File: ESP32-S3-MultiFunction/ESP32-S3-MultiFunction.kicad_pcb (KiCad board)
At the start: 2 copper layers, 99.1 x 125.7 mm, 140 parts, among them IC1 ESP32-S3-WROOM-1U-N8, IC2 USBLC6-2SC6, J1 USB_C, J501 -SM+, J801 RJ45, J802 RJ45, P701 A7 A6 A5 A4 A3 A2 A1 A0 C, P702 B7 B6 B5 B4 B3 B2 B1 B0 C, SW1 BOOT, SW201 RESET, T701 + 12V -, T801 - 15 in +, T802 - 15 out +, U301 LM2574N-3.3, U401 TC4426, U402 TC4426, U403 74HCT14, U501 74HCT00, U502 74HCT00, U503 TC4428, U504 TC4428, U505 TC4428, U506 TC4428, U601 LM339, U602 LM339, U701 PCA9685, U702 TBD62X83A, U703 TBD62X83A, U801 TCAN332DR

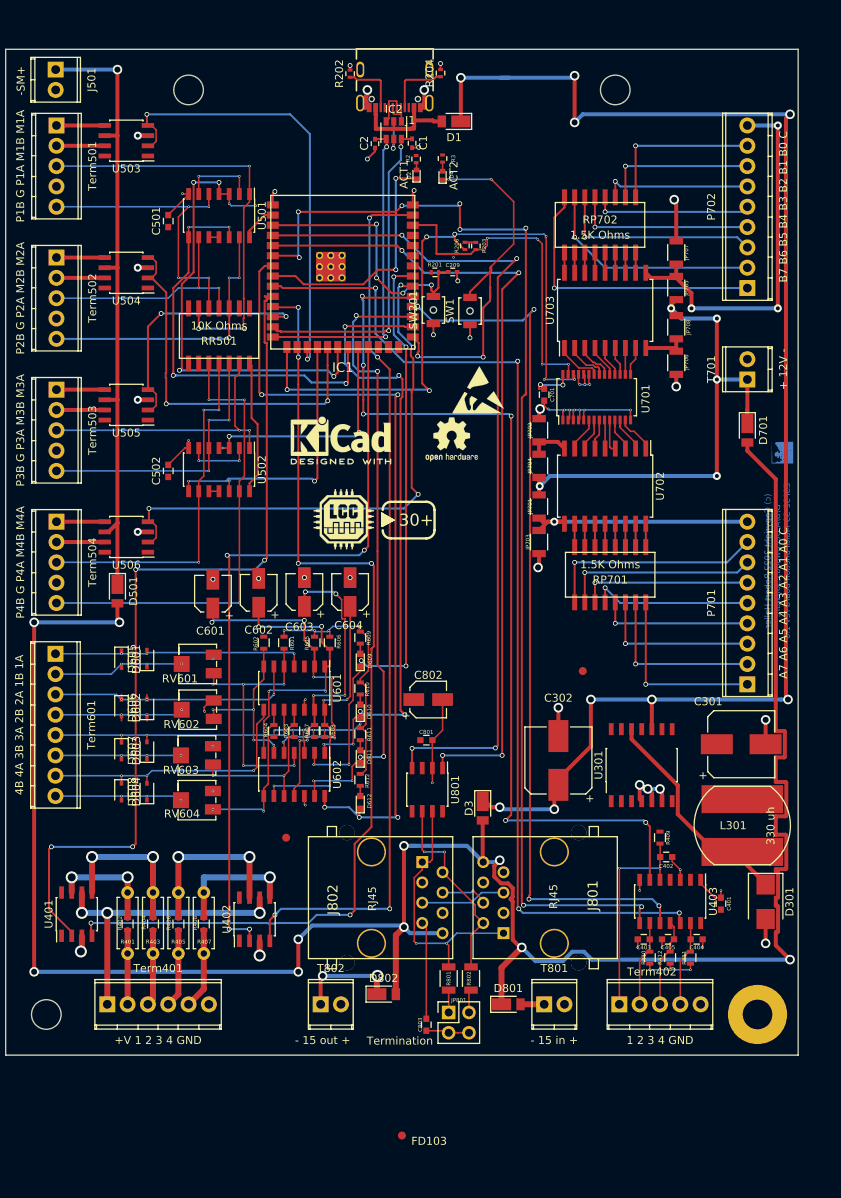
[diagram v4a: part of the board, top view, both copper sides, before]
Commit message: Revert to chip version, USB-C, replace reset and boot buttons.
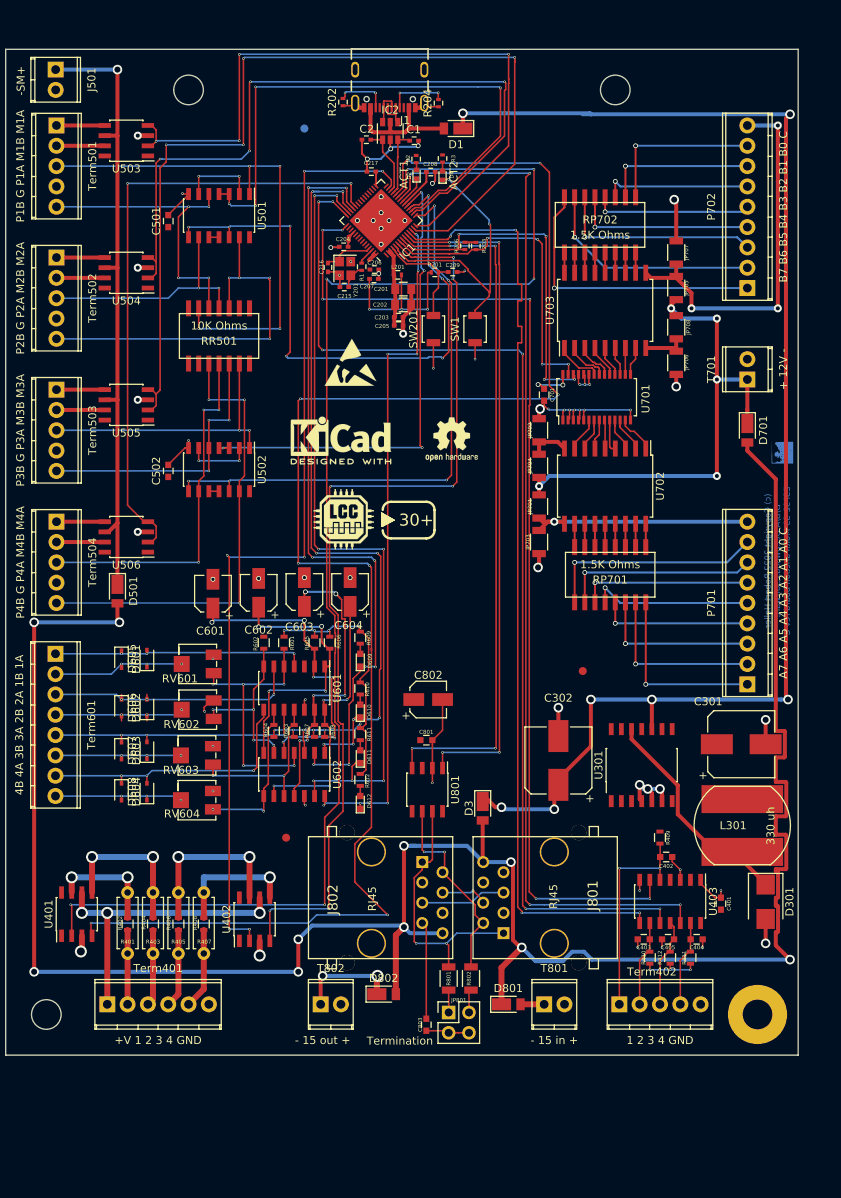
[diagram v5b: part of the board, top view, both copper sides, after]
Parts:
- added C201: 10uf, Capacitors_SMD:C_0805, F.Cu at (123.4, 55.4)
- added C202: 10uf, Capacitors_SMD:C_0805, F.Cu at (123.3, 57.4)
- added C203: 1uf, Capacitors_SMD:C_0402, F.Cu at (122.8, 58.9)
- added C204: 100nf, Capacitors_SMD:C_0402, F.Cu at (115.9, 50.1)
- added C205: 100nf, Capacitors_SMD:C_0402, F.Cu at (122.8, 59.9)
- added C206: 1uf, Capacitors_SMD:C_0402, F.Cu at (119.7, 52.9)
- added C207: 100pf, Capacitors_SMD:C_0402, F.Cu at (119.7, 54.1)
- added C208: 100nf, Capacitors_SMD:C_0402, F.Cu at (126.8, 40.7)
- added C215: 22pf, Capacitors_SMD:C_0402, F.Cu at (116.0, 55.1)
- added C216: 22pf, Capacitors_SMD:C_0402, F.Cu at (113.9, 52.7)
- added C217: 1uf, Capacitors_SMD:C_0402, F.Cu at (119.4, 40.7)
- added L201: 2.0nH, Inductors_SMD:L_0402, F.Cu at (122.7, 53.6)
- added R1: 0, Resistors_SMD:R_0402, F.Cu at (118.2, 52.6)
- added Y201: 40 Mhz +/- 10 ppm, FA_20H:FA20_H, F.Cu at (116.1, 52.8)
- FD103: moved to B.Cu
- IC1: value ESP32-S3-WROOM-1U-N8 -> ESP32-S3FN8; footprint ESP32-S3-WROOM:ESP32_S3_WROOM-1U -> Housings_DFN_QFN:QFN-56-1EP_7x7mm_Pitch0.4mm
- SW1, SW201: footprint Buttons_Switches_SMD:SW_SPST_B3U-1000P-B -> Buttons_Switches_SMD:SW_SPST_B3U-1000P
- moved FD103 126.5 mm to (111.0, 35.3)
- moved REF*** 16.3 mm to (116.8, 64.5)
- moved IC1 8.43 mm to (120.6, 46.8), turned to 135 degrees
- moved R204 3.76 mm to (127.8, 32.1)
- moved R202 3.67 mm to (115.8, 32.0)
- moved SW201 2.38 mm to (127.1, 60.4)
- moved SW1 2.34 mm to (132.3, 60.4)
- moved C2 1.18 mm to (118.7, 36.7), turned to 180 degrees
- moved D1 0.92 mm to (130.0, 35.3)
- moved J1 0.64 mm to (121.7, 28.0)
- moved IC2 0.45 mm to (121.7, 35.6)
- moved C1 0.41 mm to (124.7, 36.8), turned to 180 degrees
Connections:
- D609 pad 1: /ESP32 MCU/GPIO40(OD1) -> /ESP32 MCU/GPIO34(OD1)
- IC1 pad 1: GND -> Net-(IC1-Pad1)
- IC1 pad 10: /ESP32 MCU/GPIO17(LEDS1) -> /CAN Tranceiver/CAN_TX
- IC1 pad 11: /ESP32 MCU/GPIO18(LEDS2) -> /Buttons and LEDs/Button2
- IC1 pad 12: /ESP32 MCU/GPIO8(Motor3) -> /ESP32 MCU/GPIO7(OD4)
- IC1 pad 13: /ESP32 MCU/D- -> /ESP32 MCU/GPIO8(Motor3)
- IC1 pad 14: /ESP32 MCU/D+ -> /ESP32 MCU/GPIO9(Motor1)
- IC1 pad 15: /ESP32 MCU/SCL -> /ESP32 MCU/GPIO10(Points4)
- IC1 pad 16: Net-(IC1-Pad16) -> /ESP32 MCU/GPIO11(Motor2)
- IC1 pad 17: /ESP32 MCU/GPIO9(Motor1) -> /ESP32 MCU/GPIO12(Points1)
- IC1 pad 18: /ESP32 MCU/GPIO10(Points4) -> /ESP32 MCU/GPIO13(Points2)
- IC1 pad 19: /ESP32 MCU/GPIO11(Motor2) -> /ESP32 MCU/GPIO14(Points3)
- IC1 pad 2: +3V3 -> /ESP32 MCU/VDD3P3
- IC1 pad 20: /ESP32 MCU/GPIO12(Points1) -> +3V3
- IC1 pad 21: /ESP32 MCU/GPIO13(Points2) -> /ESP32 MCU/GPIO15(Act1)
- IC1 pad 22: /ESP32 MCU/GPIO14(Points3) -> /Buttons and LEDs/Button4
- IC1 pad 23: /ESP32 MCU/GPIO21(LEDS3) -> /ESP32 MCU/GPIO17(LEDS1)
- IC1 pad 24: Net-(IC1-Pad24) -> /ESP32 MCU/GPIO18(LEDS2)
- IC1 pad 25: Net-(IC1-Pad25) -> /ESP32 MCU/D-
- IC1 pad 26: Net-(IC1-Pad26) -> /ESP32 MCU/D+
- IC1 pad 27: /ESP32 MCU/GPIO0(Act2) -> /ESP32 MCU/GPIO21(LEDS3)
- IC1 pad 28: /ESP32 MCU/GPIO35(OD2) -> Net-(IC1-Pad28)
- IC1 pad 29: /ESP32 MCU/GPIO36(OD3) -> Net-(C217-Pad1)
- IC1 pad 3: /ESP32 MCU/RESET -> /ESP32 MCU/VDD3P3
- IC1 pad 30: /Buttons and LEDs/Button3 -> Net-(IC1-Pad30)
- IC1 pad 31: /Buttons and LEDs/Button1 -> Net-(IC1-Pad31)
- IC1 pad 32: /ESP32 MCU/GPIO39(Motor4) -> Net-(IC1-Pad32)
- IC1 pad 33: /ESP32 MCU/GPIO40(OD1) -> Net-(IC1-Pad33)
- IC1 pad 38: /ESP32 MCU/SDA -> /ESP32 MCU/GPIO33(Motor4)
- IC1 pad 39: /ESP32 MCU/GPIO1(LEDS4) -> /ESP32 MCU/GPIO34(OD1)
- IC1 pad 4: /CAN Tranceiver/CAN_RX -> /ESP32 MCU/RESET
- IC1 pad 40: GND -> /ESP32 MCU/GPIO35(OD2)
- IC1 pad 5: /CAN Tranceiver/CAN_TX -> /ESP32 MCU/GPIO0(Act2)
- IC1 pad 6: /Buttons and LEDs/Button2 -> /ESP32 MCU/GPIO1(LEDS4)
- IC1 pad 7: /ESP32 MCU/GPIO7(OD4) -> /ESP32 MCU/SDA
- IC1 pad 8: /ESP32 MCU/GPIO15(Act1) -> /ESP32 MCU/SCL
- IC1 pad 9: /Buttons and LEDs/Button4 -> /CAN Tranceiver/CAN_RX
- R202 pad 1: Net-(J1-PadB5) -> GND
- R202 pad 2: GND -> Net-(J1-PadB5)
- R204 pad 1: Net-(J1-PadA5) -> GND
- R204 pad 2: GND -> Net-(J1-PadA5)
- U506 pad 2: /ESP32 MCU/GPIO39(Motor4) -> /ESP32 MCU/GPIO33(Motor4)
- U506 pad 4: /ESP32 MCU/GPIO39(Motor4) -> /ESP32 MCU/GPIO33(Motor4)
- U602 pad 2: /ESP32 MCU/GPIO40(OD1) -> /ESP32 MCU/GPIO34(OD1)
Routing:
- net /ESP32 MCU/GPIO34(OD1): track 0.00 -> 96.2 mm, vias 0 -> 8
- net /ESP32 MCU/GPIO8(Motor3): track 31.6 -> 119.8 mm, vias 2 -> 4
- net /ESP32 MCU/GPIO33(Motor4): track 0.00 -> 78.6 mm, vias 0 -> 2
- net /ESP32 MCU/GPIO40(OD1): track 77.1 -> 0.00 mm, vias 6 -> 0
- net /ESP32 MCU/GPIO18(LEDS2): track 124.4 -> 199.7 mm, vias 6 -> 8
- net /ESP32 MCU/GPIO39(Motor4): track 70.0 -> 0.00 mm, vias 4 -> 0
- net /ESP32 MCU/GPIO17(LEDS1): track 108.7 -> 175.4 mm, vias 4 -> 6
- net /ESP32 MCU/GPIO11(Motor2): track 47.6 -> 91.3 mm, vias 2 -> 4
- net /ESP32 MCU/SCL: track 83.8 -> 44.3 mm, vias 7 -> 4
- net /ESP32 MCU/GPIO10(Points4): track 36.0 -> 73.1 mm, vias 3 -> 5
- net /ESP32 MCU/D-: track 40.8 -> 8.45 mm, vias 2 -> 0
- net /ESP32 MCU/D+: track 40.6 -> 8.80 mm, vias 2 -> 0
- net GND: track 134.1 -> 165.7 mm, vias 57 -> 65
- net /ESP32 MCU/GPIO14(Points3): track 30.0 -> 61.3 mm, vias 3 -> 4
- net /ESP32 MCU/GPIO9(Motor1): track 56.6 -> 86.1 mm, vias 2 -> 4
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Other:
- board text added: "(c) Copyright 2022 Robert Heller D/B/A Deepwoods Software ESP32-S3-MultiFunction board rev C"
- board text removed: "(c) Copyright 2022 Robert Heller D/B/A Deepwoods Software ESP32-S3-MultiFunction board rev 1.0"

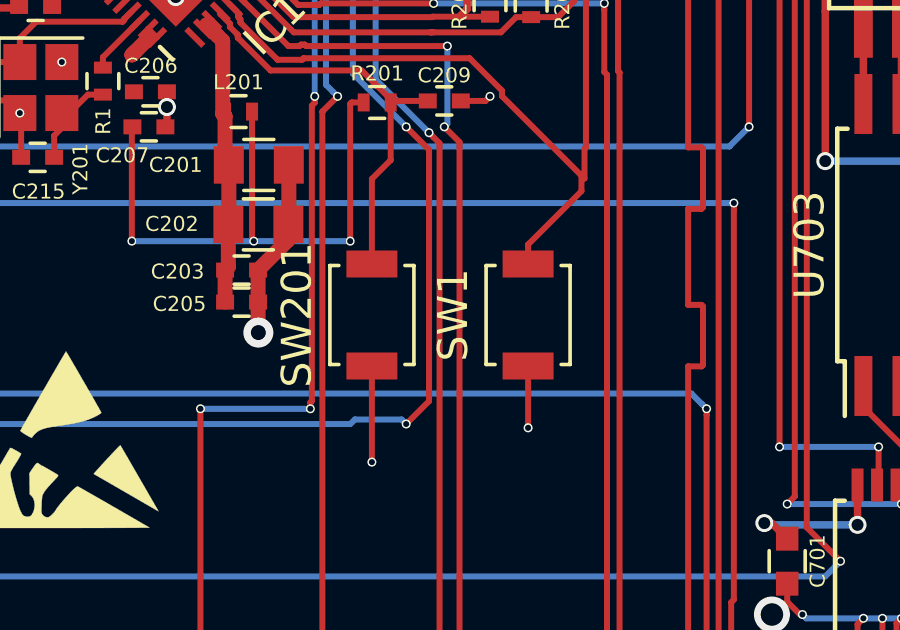
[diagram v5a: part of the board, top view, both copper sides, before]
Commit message: Update Boot and reset switches.
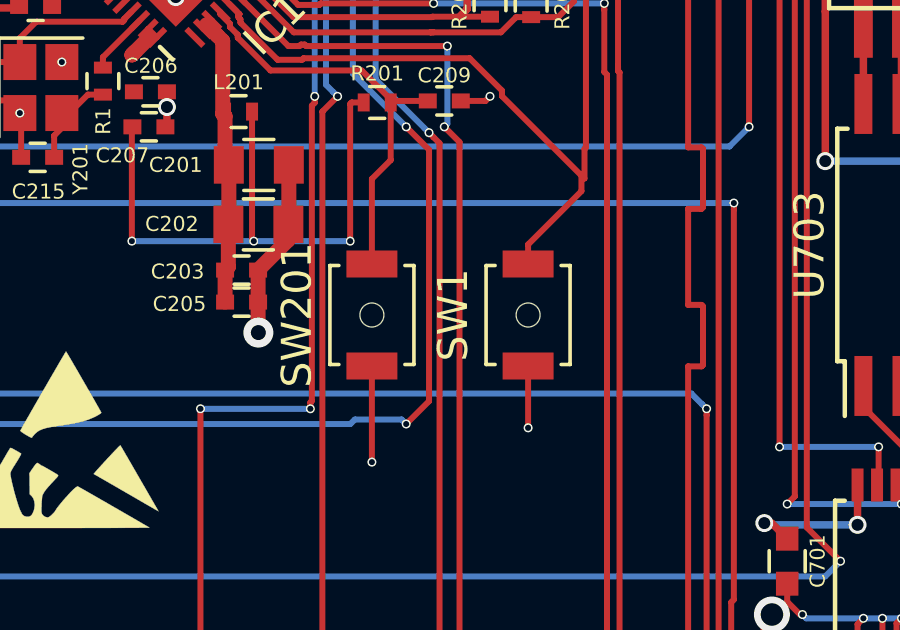
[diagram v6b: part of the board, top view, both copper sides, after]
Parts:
- SW1, SW201: footprint Buttons_Switches_SMD:SW_SPST_B3U-1000P -> Buttons_Switches_SMD:SW_SPST_B3U-1000P-B
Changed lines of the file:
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@@
   )
   (setup
-    (last_trace_width 0.5)
+    (last_trace_width 0.25)
     (user_trace_width 0.2)
     (user_trace_width 0.5)
@@
     )
   )
-  (module Buttons_Switches_SMD:SW_SPST_B3U-1000P (layer F.Cu)
+  (module Buttons_Switches_SMD:SW_SPST_B3U-1000P-B (layer F.Cu)
     (at 132.334 60.374 90)
-    (descr "Ultra-small-sized Tactile Switch with High Contact Reliability, Top-actuated Model, without Ground Terminal, without Boss")
+    (descr "Ultra-small-sized Tactile Switch with High Contact Reliability, Top-actuated Model, without Ground Terminal, with Boss")
     (tags "Tactile Switch")
     (attr smd)
@@
     (pad 2 smd rect (at 1.7 0 90) (size 0.9 1.7) (layers F.Cu F.Paste F.Mask)
       (net 192 "/ESP32 MCU/GPIO0(Act2)"))
-    (model ${KISYS3DMOD}/Buttons_Switches_SMD.3dshapes/SW_SPST_B3U-1000P.wrl
+    (pad "" np_thru_hole circle (at 0 0 90) (size 0.8 0.8) (drill 0.8) (layers *.Cu *.Mask))
+    (model ${KISYS3DMOD}/Buttons_Switches_SMD.3dshapes/SW_SPST_B3U-1000P-B.wrl
       (at (xyz 0 0 0))
       (scale (xyz 1 1 1))
@@
     )
   )
-  (module Buttons_Switches_SMD:SW_SPST_B3U-1000P (layer F.Cu)
+  (module Buttons_Switches_SMD:SW_SPST_B3U-1000P-B (layer F.Cu)
     (at 127.127 60.374 90)
-    (descr "Ultra-small-sized Tactile Switch with High Contact Reliability, Top-actuated Model, without Ground Terminal, without Boss")
+    (descr "Ultra-small-sized Tactile Switch with High Contact Reliability, Top-actuated Model, without Ground Terminal, with Boss")
     (tags "Tactile Switch")
     (attr smd)
@@
     (pad 2 smd rect (at 1.7 0 90) (size 0.9 1.7) (layers F.Cu F.Paste F.Mask)
       (net 4 "/ESP32 MCU/RESET"))
-    (model ${KISYS3DMOD}/Buttons_Switches_SMD.3dshapes/SW_SPST_B3U-1000P.wrl
+    (pad "" np_thru_hole circle (at 0 0 90) (size 0.8 0.8) (drill 0.8) (layers *.Cu *.Mask))
+    (model ${KISYS3DMOD}/Buttons_Switches_SMD.3dshapes/SW_SPST_B3U-1000P-B.wrl
       (at (xyz 0 0 0))
       (scale (xyz 1 1 1))
